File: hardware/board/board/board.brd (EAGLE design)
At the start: 64.8 x 100 mm, 7 parts, among them M1 WIRELESS-NRF24L01, X1 MAB7SH

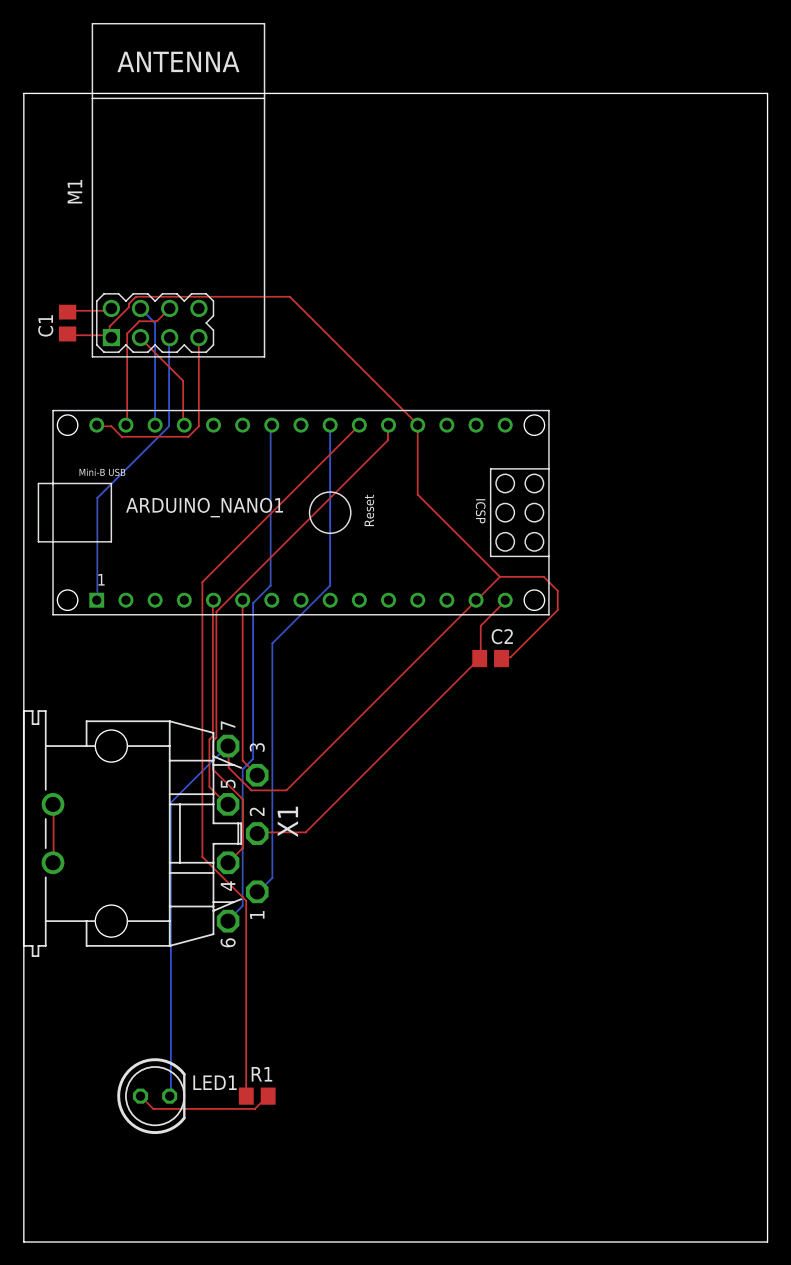
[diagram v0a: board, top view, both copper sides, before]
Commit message: added arduino hardware
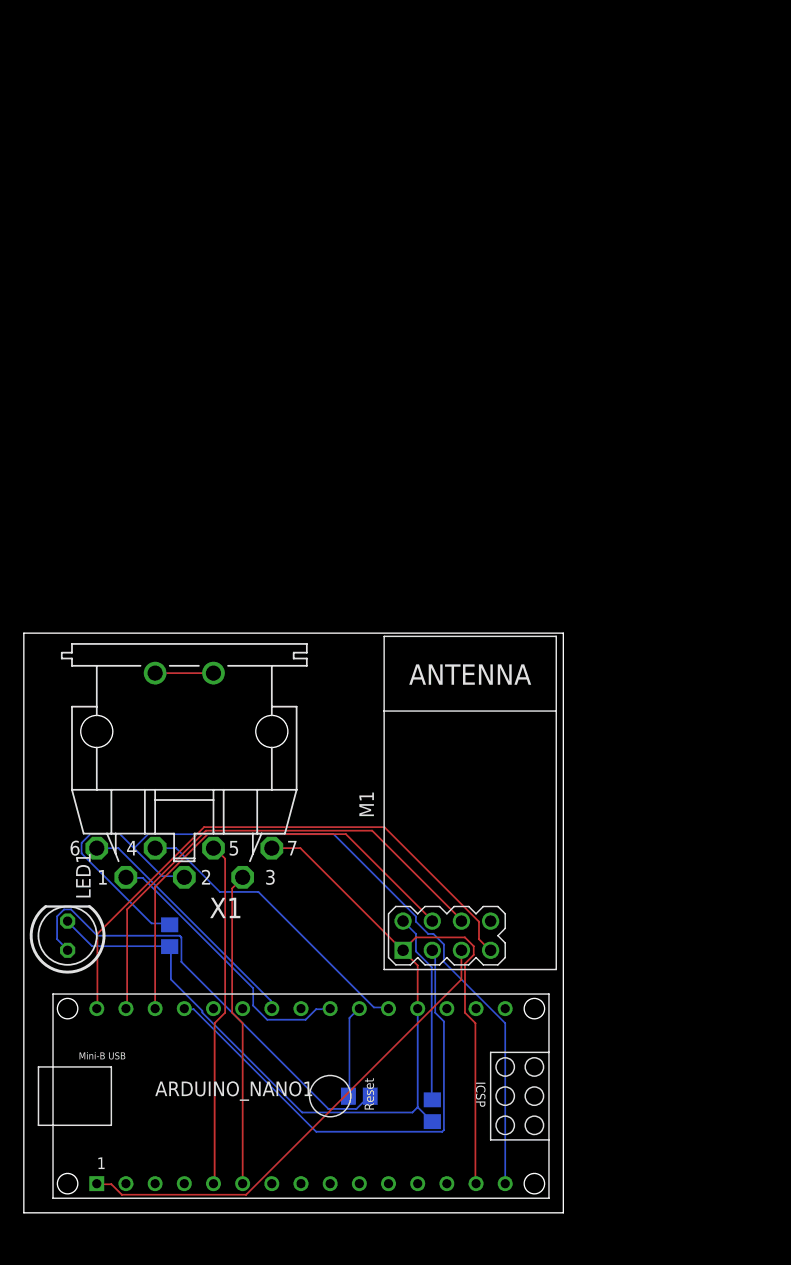
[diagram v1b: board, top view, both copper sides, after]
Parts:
- moved C1 75.6 mm to (35.6, 11.4), flipped to the bottom
- moved M1 59.1 mm to (39.4, 38.1)
- moved ARDUINO_NANO1 50.8 mm to (26.7, 12.7)
- moved C2 36.9 mm to (12.7, 26.7), flipped to the bottom, turned to 270 degrees
- moved LED1 15.9 mm to (3.81, 26.7), turned to 90 degrees
- moved X1 10.9 mm to (14.0, 44.5), turned to 180 degrees
- moved R1 8.89 mm to (29.2, 12.7), flipped to the bottom, turned to 180 degrees
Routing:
- net N$7: track 65.7 -> 8.03 mm
- net VIN: track 31.7 -> 76.8 mm
- net GND: track 134.5 -> 98.7 mm
- net N$5: track 9.21 -> 43.2 mm
- net N$2: track 17.4 -> 49.9 mm
- net N$3: track 12.7 -> 43.9 mm
- net N$4: track 10.7 -> 39.8 mm
- net N$6: track 12.0 -> 39.7 mm
- net N$8: track 44.7 -> 21.4 mm
- net N$12: track 46.0 -> 26.1 mm
- net N$10: track 43.3 -> 24.2 mm
- net N$1: track 25.5 -> 42.5 mm
- net 3V3: track 4.04 -> 16.6 mm
- net N$9: track 15.8 -> 27.4 mm
- net N$11: track 18.7 -> 30.1 mm
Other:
- board size 64.8 x 100 mm -> 47 x 50.5 mm

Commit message: value update
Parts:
- R1: value (none) -> 220
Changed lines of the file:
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@@
 <drawing>
 <settings>
-<setting alwaysvectorfont="yes"/>
+<setting alwaysvectorfont="no"/>
 <setting verticaltext="up"/>
 </settings>
@@
 <attribute name="VALUE" x="46.99" y="38.1" size="1.27" layer="27" rot="R90" align="top-center"/>
 </element>
-<element name="R1" library="rcl" library_urn="urn:adsk.eagle:library:334" package="R0805" package3d_urn="urn:adsk.eagle:package:23553/2" value="" x="29.21" y="12.7" smashed="yes" rot="MR180">
+<element name="R1" library="rcl" library_urn="urn:adsk.eagle:library:334" package="R0805" package3d_urn="urn:adsk.eagle:package:23553/2" value="220" x="29.21" y="12.7" smashed="yes" rot="MR180">
 <attribute name="NAME" x="31.115" y="11.43" size="1.27" layer="26" rot="MR180"/>
 <attribute name="POPULARITY" value="86" x="69.85" y="78.74" size="1.778" layer="28" rot="MR180" display="off"/>

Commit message: connected 3V3 radio line to the aruino nano
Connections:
- net 3V3: now also ARDUINO_NANO1.2
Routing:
- net 3V3: track 16.6 -> 65.3 mm, vias 0 -> 1
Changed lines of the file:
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@@
 </layers>
 <board>
-<fusionsync huburn="a.YnVzaW5lc3M6bXlteTgxOTE" projecturn="a.YnVzaW5lc3M6bXlteTgxOTEjRDIwMjEwNDExNDAxNzI2ODMx" f3durn="urn:adsk.wipprod:dm.lineage:ym6S85r8RSWroSzpIbR_yw" pcbguid="" lastpulledtime="" lastsyncedchangeguid="" latestrevisionid="9f4b6dd6-f49c-450e-a083-c3f2b52c4217" lastsyncedrevisionid="9f4b6dd6-f49c-450e-a083-c3f2b52c4217" lastboardhashguid="e0a3180f-a657-3b8e-2011-eee5726cb7fb" lastpushedtime="2021-04-12T18:14:04Z" linktopcb3d="true"/>
+<fusionsync huburn="a.YnVzaW5lc3M6bXlteTgxOTE" projecturn="a.YnVzaW5lc3M6bXlteTgxOTEjRDIwMjEwNDExNDAxNzI2ODMx" f3durn="urn:adsk.wipprod:dm.lineage:ym6S85r8RSWroSzpIbR_yw" pcbguid="" lastpulledtime="" lastsyncedchangeguid="" latestrevisionid="9f4b6dd6-f49c-450e-a083-c3f2b52c4217" lastsyncedrevisionid="9f4b6dd6-f49c-450e-a083-c3f2b52c4217" lastboardhashguid="e0a3180f-a657-3b8e-2011-eee5726cb7fb" lastpushedtime="2021-04-12T18:14:04Z" linktopcb3d="false"/>
 <plain>
 <wire x1="0" y1="2.54" x2="46.97" y2="2.54" width="0" layer="20"/>
@@
 </signal>
 <signal name="N$2">
-<contactref element="M1" pad="7"/>
 <contactref element="ARDUINO_NANO1" pad="30"/>
 <wire x1="6.4008" y1="26.8224" x2="6.4008" y2="20.4216" width="0.1524" layer="1"/>
@@
 <wire x1="6.4008" y1="20.4216" x2="6.35" y2="20.32" width="0.1524" layer="1"/>
 <wire x1="40.5384" y1="25.4508" x2="40.64" y2="25.4" width="0.1524" layer="1"/>
+<contactref element="M1" pad="7"/>
 </signal>
 <signal name="N$3">
-<contactref element="M1" pad="6"/>
 <contactref element="ARDUINO_NANO1" pad="29"/>
 <wire x1="8.9916" y1="28.956" x2="8.9916" y2="20.4216" width="0.1524" layer="1"/>
@@
 <wire x1="8.9916" y1="20.4216" x2="8.89" y2="20.32" width="0.1524" layer="1"/>
 <wire x1="38.1" y1="28.0416" x2="38.1" y2="27.94" width="0.1524" layer="1"/>
+<contactref element="M1" pad="6"/>
 </signal>
 <signal name="N$4">
-<contactref element="M1" pad="4"/>
 <contactref element="ARDUINO_NANO1" pad="28"/>
 <wire x1="11.43" y1="30.9372" x2="11.43" y2="20.32" width="0.1524" layer="1"/>
@@
 <wire x1="35.5092" y1="28.0416" x2="28.0416" y2="35.5092" width="0.1524" layer="1"/>
 <wire x1="35.5092" y1="28.0416" x2="35.56" y2="27.94" width="0.1524" layer="1"/>
+<contactref element="M1" pad="4"/>
 </signal>
 <signal name="N$1">
-<contactref element="M1" pad="5"/>
 <contactref element="ARDUINO_NANO1" pad="1"/>
 <wire x1="7.62" y1="5.0292" x2="6.4008" y2="5.0292" width="0.1524" layer="1"/>
@@
 <wire x1="38.1" y1="25.4" x2="38.1" y2="22.86" width="0.1524" layer="1"/>
 <wire x1="6.4008" y1="5.0292" x2="6.35" y2="5.08" width="0.1524" layer="1"/>
+<contactref element="M1" pad="5"/>
 </signal>
 <signal name="N$5">
-<contactref element="M1" pad="3"/>
 <contactref element="ARDUINO_NANO1" pad="27"/>
 <wire x1="14.7828" y1="20.2692" x2="14.0208" y2="20.2692" width="0.1524" layer="16"/>
@@
 <wire x1="35.56" y1="25.4" x2="35.814" y2="25.146" width="0.1524" layer="16"/>
 <wire x1="14.0208" y1="20.2692" x2="13.97" y2="20.32" width="0.1524" layer="16"/>
+<contactref element="M1" pad="3"/>
 </signal>
 <signal name="GND">
 <contactref element="ARDUINO_NANO1" pad="19"/>
 <contactref element="ARDUINO_NANO1" pad="14"/>
-<contactref element="C1" pad="1"/>
-<contactref element="M1" pad="1"/>
 <contactref element="LED1" pad="K"/>
 <contactref element="X1" pad="7"/>
@@
 <wire x1="34.29" y1="11.7348" x2="33.8328" y2="11.2776" width="0.1524" layer="16"/>
 <wire x1="12.8016" y1="25.6032" x2="12.7" y2="25.72" width="0.1524" layer="16"/>
+<contactref element="C1" pad="1"/>
+<contactref element="M1" pad="1"/>
 </signal>
 <signal name="3V3">
+<wire x1="35.5092" y1="23.9268" x2="35.5092" y2="12.4968" width="0.1524" layer="16"/>
+<wire x1="35.5092" y1="23.9268" x2="33.02" y2="26.416" width="0.1524" layer="16"/>
+<wire x1="33.02" y1="27.94" x2="33.02" y2="26.416" width="0.1524" layer="16"/>
+<wire x1="35.5092" y1="12.4968" x2="35.56" y2="12.38" width="0.1524" layer="16"/>
 <contactref element="C1" pad="2"/>
 <contactref element="M1" pad="2"/>
-<wire x1="35.5092" y1="23.9268" x2="35.5092" y2="12.4968" width="0.1524" layer="16"/>
-<wire x1="34.1376" y1="25.2984" x2="35.5092" y2="23.9268" width="0.1524" layer="16"/>
-<wire x1="34.1376" y1="26.8224" x2="34.1376" y2="25.2984" width="0.1524" layer="16"/>
-<wire x1="33.02" y1="27.94" x2="34.1376" y2="26.8224" width="0.1524" layer="16"/>
-<wire x1="35.5092" y1="12.4968" x2="35.56" y2="12.38" width="0.1524" layer="16"/>
+<contactref element="ARDUINO_NANO1" pad="2"/>
+<wire x1="8.9916" y1="16.6116" x2="8.9916" y2="5.1816" width="0.1524" layer="1"/>
+<wire x1="16.9164" y1="24.5364" x2="8.9916" y2="16.6116" width="0.1524" layer="1"/>
+<wire x1="16.9164" y1="31.5468" x2="16.9164" y2="24.5364" width="0.1524" layer="1"/>
+<wire x1="18.4404" y1="33.0708" x2="16.9164" y2="31.5468" width="0.1524" layer="16"/>
+<wire x1="27.8892" y1="33.0708" x2="18.4404" y2="33.0708" width="0.1524" layer="16"/>
+<wire x1="33.02" y1="27.94" x2="27.8892" y2="33.0708" width="0.1524" layer="16"/>
+<wire x1="8.9916" y1="5.1816" x2="8.89" y2="5.08" width="0.1524" layer="1"/>
+<via x="16.9164" y="31.5468" extent="1-16" drill="0.35"/>
 </signal>
 <signal name="N$6">
